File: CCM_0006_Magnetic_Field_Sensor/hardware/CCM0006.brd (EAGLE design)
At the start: 63.5 x 95.2 mm, 28 parts, among them IC1 AD654, IC2 AD820R, IC3 AD820R

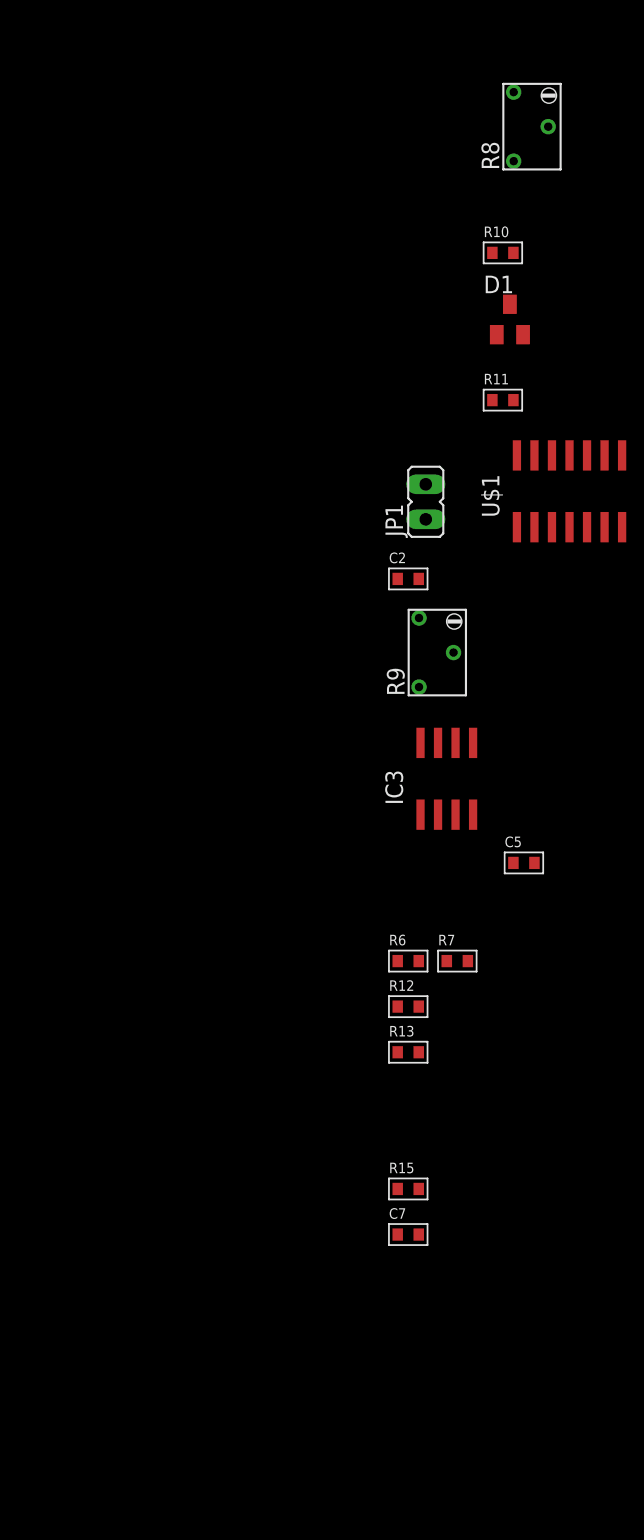
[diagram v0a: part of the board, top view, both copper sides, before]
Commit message: fixed stepper motor firmware bug with parameter saving (v1.5)
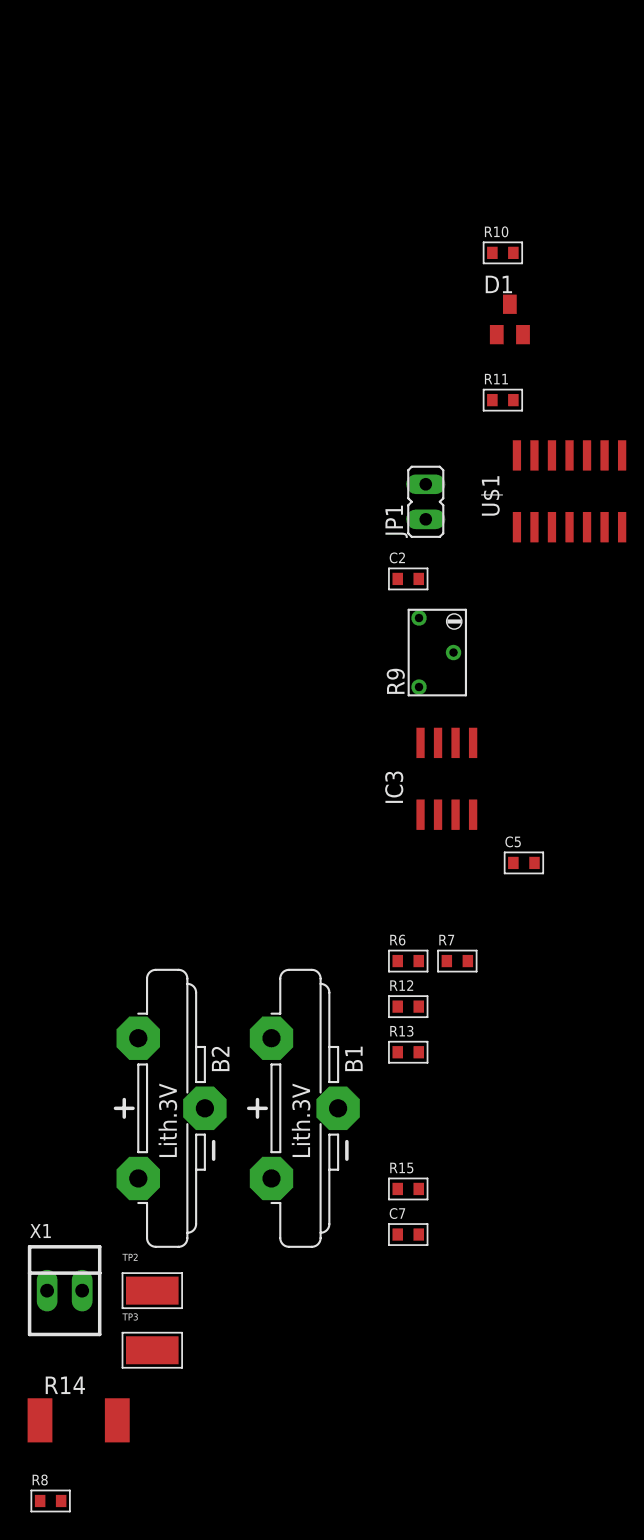
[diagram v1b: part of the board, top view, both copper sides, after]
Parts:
- added B1, B2: CR2032V, battery:CR2032V
- added R14: 1k, noah:2512
- added TP2, TP3: TESTPOINT, Fitch:TESTPOINT
- added X1: 22-23-2021, con-molex:22-23-2021
- R8: value (none) -> 10k; device rcl:RTRIM74W -> ic:0603
- moved R8 105.5 mm to (-48.3, -155.4)
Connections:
- removed net N$19: R13.2, R8.2
- new net N$20: B1.+, B2.-
- new net N$21: R14.1, X1.1
- net AGND: now also B1.-, TP3.P$1, X1.2
- net N$11: now also R13.2, R8.2; no longer R8.3
- net VCC: now also B2.+, R14.2, TP2.P$1
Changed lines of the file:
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@@
 <element name="R4" library="ic" package="0603" value="51k" x="-15.494" y="-40.64"/>
 <element name="R5" library="ic" package="0603" value="1k" x="-15.494" y="-43.942"/>
-<element name="R8" library="rcl" package="RTRIM74W" value="" x="-13.462" y="-55.88"/>
 <element name="R10" library="ic" package="0603" value="10k" x="-15.494" y="-65.024"/>
 <element name="D1" library="Fitch" package="SOT23" value="LM4040" x="-14.986" y="-69.85"/>
@@
 <element name="R15" library="ic" package="0603" value="10k" x="-22.352" y="-132.842"/>
 <element name="C7" library="ic" package="0603" value="0.1u" x="-22.352" y="-136.144"/>
+<element name="B1" library="battery" package="CR2032V" value="CR2032V" x="-29.718" y="-127"/>
+<element name="B2" library="battery" package="CR2032V" value="CR2032V" x="-39.37" y="-127"/>
+<element name="TP2" library="Fitch" package="TESTPOINT" value="TESTPOINT" x="-40.894" y="-140.208"/>
+<element name="TP3" library="Fitch" package="TESTPOINT" value="TESTPOINT" x="-40.894" y="-144.526"/>
+<element name="X1" library="con-molex" package="22-23-2021" value="22-23-2021" x="-47.244" y="-140.208">
+<attribute name="OC_NEWARK" value="25C3832" x="-47.244" y="-140.208" size="1.778" layer="27" display="off"/>
+<attribute name="MPN" value="22-23-2021" x="-47.244" y="-140.208" size="1.778" layer="27" display="off"/>
+<attribute name="MF" value="MOLEX" x="-47.244" y="-140.208" size="1.778" layer="27" display="off"/>
+<attribute name="OC_FARNELL" value="1462926" x="-47.244" y="-140.208" size="1.778" layer="27" display="off"/>
+</element>
+<element name="R14" library="noah" package="2512" value="1k" x="-46.228" y="-149.606"/>
+<element name="R8" library="ic" package="0603" value="10k" x="-48.26" y="-155.448"/>
 </elements>
 <signals>
@@
 <contactref element="R5" pad="1"/>
 <contactref element="D1" pad="2"/>
-<contactref element="R8" pad="1"/>
 <contactref element="C2" pad="2"/>
 <contactref element="U$1" pad="4"/>
@@
 <contactref element="R7" pad="1"/>
 <contactref element="C7" pad="1"/>
-<wire x1="-19.558" y1="-116.332" x2="-23.114" y2="-136.144" width="0" layer="19" extent="1-1"/>
+<contactref element="B1" pad="-"/>
+<contactref element="TP3" pad="P$1"/>
+<contactref element="X1" pad="2"/>
+<contactref element="R8" pad="1"/>
+<wire x1="-40.894" y1="-144.526" x2="-49.022" y2="-155.448" width="0" layer="19" extent="1-1"/>
+<wire x1="-45.974" y1="-140.208" x2="-40.894" y2="-144.526" width="0" layer="19" extent="1-1"/>
+<wire x1="-23.114" y1="-136.144" x2="-40.894" y2="-144.526" width="0" layer="19" extent="1-1"/>
+<wire x1="-27.432" y1="-127" x2="-23.114" y2="-136.144" width="0" layer="19" extent="1-1"/>
+<wire x1="-19.558" y1="-116.332" x2="-27.432" y2="-127" width="0" layer="19" extent="1-1"/>
 <wire x1="-13.208" y1="-109.22" x2="-19.558" y2="-116.332" width="0" layer="19" extent="1-1"/>
 <wire x1="-17.653" y1="-105.724" x2="-13.208" y2="-109.22" width="0" layer="19" extent="1-1"/>
@@
 <wire x1="-10.668" y1="-84.896" x2="-21.082" y2="-84.328" width="0" layer="19" extent="1-1"/>
 <wire x1="-14.036" y1="-70.95" x2="-10.668" y2="-84.896" width="0" layer="19" extent="1-1"/>
-<wire x1="-14.712" y1="-58.38" x2="-14.036" y2="-70.95" width="0" layer="19" extent="1-1"/>
-<wire x1="-16.256" y1="-43.942" x2="-14.712" y2="-58.38" width="0" layer="19" extent="1-1"/>
+<wire x1="-16.256" y1="-43.942" x2="-14.036" y2="-70.95" width="0" layer="19" extent="1-1"/>
 <wire x1="-14.732" y1="-37.338" x2="-16.256" y2="-43.942" width="0" layer="19" extent="1-1"/>
 <wire x1="-14.712" y1="-33.996" x2="-14.732" y2="-37.338" width="0" layer="19" extent="1-1"/>
@@
 <contactref element="IC3" pad="7"/>
 <contactref element="C5" pad="1"/>
+<contactref element="B2" pad="+"/>
+<contactref element="TP2" pad="P$1"/>
+<contactref element="R14" pad="2"/>
+<wire x1="-40.894" y1="-140.208" x2="-43.428" y2="-149.606" width="0" layer="19" extent="1-1"/>
+<wire x1="-41.91" y1="-132.08" x2="-40.894" y2="-140.208" width="0" layer="19" extent="1-1"/>
+<wire x1="-14.732" y1="-109.22" x2="-41.91" y2="-132.08" width="0" layer="19" extent="1-1"/>
 <wire x1="-20.193" y1="-100.524" x2="-14.732" y2="-109.22" width="0" layer="19" extent="1-1"/>
 <wire x1="-23.114" y1="-88.646" x2="-20.193" y2="-100.524" width="0" layer="19" extent="1-1"/>
@@
 </signal>
 <signal name="N$11">
-<contactref element="R8" pad="3"/>
 <contactref element="R10" pad="1"/>
-<wire x1="-14.712" y1="-53.38" x2="-16.256" y2="-65.024" width="0" layer="19" extent="1-1"/>
+<contactref element="R13" pad="2"/>
+<contactref element="R8" pad="2"/>
+<wire x1="-21.59" y1="-122.936" x2="-47.498" y2="-155.448" width="0" layer="19" extent="1-1"/>
+<wire x1="-16.256" y1="-65.024" x2="-21.59" y2="-122.936" width="0" layer="19" extent="1-1"/>
 </signal>
 <signal name="N$14">
@@
 <wire x1="-18.923" y1="-105.724" x2="-23.114" y2="-119.634" width="0" layer="19" extent="1-1"/>
 </signal>
-<signal name="N$19">
-<contactref element="R8" pad="2"/>
-<contactref element="R13" pad="2"/>
-<wire x1="-12.212" y1="-55.88" x2="-21.59" y2="-122.936" width="0" layer="19" extent="1-1"/>
-</signal>
 <signal name="N$10">
 <contactref element="C7" pad="2"/>
@@
 <wire x1="-2.921" y1="1.21" x2="-23.114" y2="-132.842" width="0" layer="19" extent="1-1"/>
 </signal>
+<signal name="N$20">
+<contactref element="B1" pad="+"/>
+<contactref element="B2" pad="-"/>
+<wire x1="-37.084" y1="-127" x2="-32.258" y2="-132.08" width="0" layer="19" extent="1-1"/>
+</signal>
+<signal name="N$21">
+<contactref element="X1" pad="1"/>
+<contactref element="R14" pad="1"/>
+<wire x1="-48.514" y1="-140.208" x2="-49.028" y2="-149.606" width="0" layer="19" extent="1-1"/>
+</signal>
 </signals>
